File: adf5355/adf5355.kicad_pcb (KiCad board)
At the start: 4 copper layers, 48.3 x 48.3 mm, 96 parts, among them J1 REF_IN_A, J2 RF_B, J3 RF_A_P, J4 REF_IN_B, J5 RF_A_N, J6 Conn_01x02_Male, J7 Conn_01x10_Male, U1 L7806, U2 ADM7150, U3 ADM7150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

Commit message: Added some capacitors, better power planes etc. Needs fixing transmission lines and checking component placement for solderability. Also the c_reg capacitors probably needs to be closer to the pin
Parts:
- added C62: 10p, Capacitors_SMD:C_0603, F.Cu at (108.1, 115.0)
- added C63: 100p, Capacitors_SMD:C_0603, F.Cu at (109.0, 118.7)
- added C64: 10n, Capacitors_SMD:C_0603, F.Cu at (116.6, 115.1)
- added C65: 10p, Capacitors_SMD:C_0603, F.Cu at (107.3, 117.2)
- added C66: 100p, Capacitors_SMD:C_0603, F.Cu at (117.3, 117.2)
- added C67: 10n, Capacitors_SMD:C_0603, F.Cu at (115.8, 118.6)
- C37: footprint Capacitors_SMD:C_0805 -> Capacitors_SMD:C_0603
- C38, L3: moved to F.Cu
- moved L3 3.79 mm to (114.5, 116.5), turned to 180 degrees
- moved C38 3.15 mm to (113.2, 85.8)
- moved C32 3.08 mm to (112.0, 85.8)
- moved C34 2.46 mm to (111.8, 122.0), turned to 90 degrees
- moved C41 2.23 mm to (113.0, 122.0), turned to 90 degrees
- moved R3 2.17 mm to (112.6, 83.6)
- moved L2 1.93 mm to (110.1, 116.5)
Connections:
- net Net-(C31-Pad1) renamed /REF2+
- net Net-(C31-Pad2) renamed /REF+
- net Net-(C32-Pad1) renamed /REF3+
- net Net-(C34-Pad2) renamed /RF_OUT+
- net Net-(C37-Pad1) renamed /REF2-
- net Net-(C37-Pad2) renamed /REF-
- net Net-(C38-Pad1) renamed /REF3-
- net Net-(C41-Pad2) renamed /RF_OUT-
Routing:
- net GND: track 365.8 -> 383.7 mm, vias 63 -> 69
- net /3V3: track 141.9 -> 156.4 mm, vias 12 -> 18
- net /RF_OUT+: track 23.1 -> 19.7 mm
- net Net-(C34-Pad1): track 5.60 -> 8.70 mm
- net Net-(C41-Pad1): track 6.35 -> 9.21 mm
- net /RF_OUT-: track 23.0 -> 20.4 mm, vias 2 -> 0
- net /REF2-: track 5.61 -> 3.18 mm, vias 1 -> 0
- net /5V: track 99.2 -> 101.6 mm, vias 8 -> 7
- net /REF2+: track 5.48 -> 3.16 mm
- net /REF3-: track 11.5 -> 13.5 mm, vias 1 -> 0
- net /REF3+: track 11.7 -> 13.6 mm
- net /REF-: track 5.48 -> 6.09 mm
- net /REF+: track 5.62 -> 6.24 mm

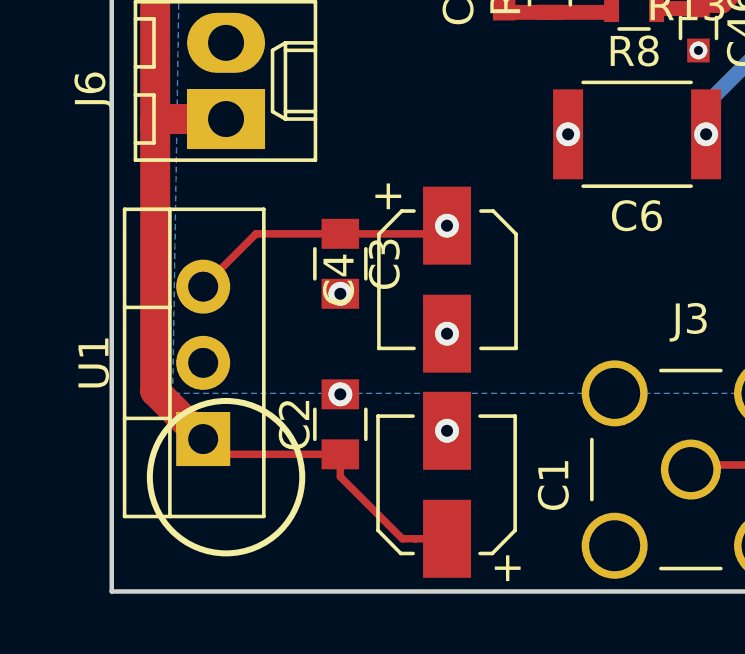
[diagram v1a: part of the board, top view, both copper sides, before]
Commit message: Added power plane for coarse input regulator
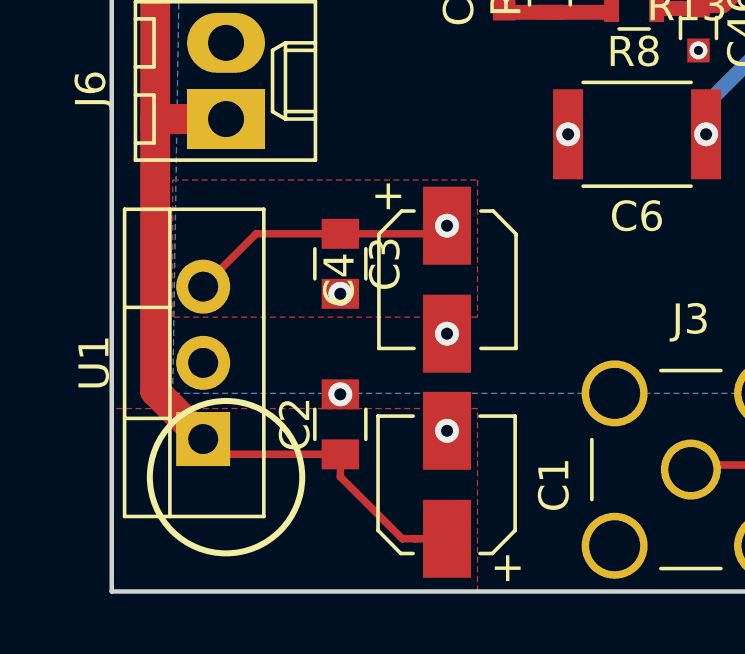
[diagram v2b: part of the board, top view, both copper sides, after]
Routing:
- added copper zone on F.Cu, net /6V
- added copper zone on F.Cu, net /VIN
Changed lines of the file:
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@@
+    )
+  )
+  (zone (net 3) (net_name /6V) (layer F.Cu) (hatch edge 0.508)
+    (connect_pads (clearance 0.2))
+    (min_thickness 0.254)
+    (fill yes (arc_segments 16) (thermal_gap 0.508) (thermal_bridge_width 0.508))
+    (polygon
+      (pts
+        (xy 96.012 113.284) (xy 96.012 117.856) (xy 85.852 117.856) (xy 85.852 113.284)
+      )
+    )
+  )
+  (zone (net 1) (net_name /VIN) (layer F.Cu) (hatch edge 0.508)
+    (connect_pads (clearance 0.2))
+    (min_thickness 0.254)
+    (fill yes (arc_segments 16) (thermal_gap 0.508) (thermal_bridge_width 0.508))
+    (polygon
+      (pts
+        (xy 83.82 127) (xy 96.012 127) (xy 96.012 120.904) (xy 83.82 120.904)
+      )
     )
   )
